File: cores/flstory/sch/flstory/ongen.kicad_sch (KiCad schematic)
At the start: 25 parts, among them M14 74LS273, M20 74LS139, M21 74LS32, M28 YM2149, M29 MSM5232RS, M33 74LS273, M34 74LS273

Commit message: jt5232: wip
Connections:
- net ~{GTWR} renamed ~{MSM}
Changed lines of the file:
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@@
 	)
 	(bus_entry
-		(at 140.335 86.36)
-		(size -2.54 2.54)
+		(at 140.335 78.74)
+		(size -2.54 -2.54)
 		(stroke
 			(width 0)
@@
 	)
 	(bus_entry
-		(at 140.335 78.74)
-		(size -2.54 2.54)
+		(at 140.335 86.36)
+		(size -2.54 -2.54)
 		(stroke
 			(width 0)
@@
 	)
 	(bus_entry
-		(at 140.335 83.82)
-		(size -2.54 2.54)
+		(at 140.335 81.28)
+		(size -2.54 -2.54)
 		(stroke
 			(width 0)
@@
 	)
 	(bus_entry
-		(at 140.335 81.28)
-		(size -2.54 2.54)
+		(at 140.335 83.82)
+		(size -2.54 -2.54)
 		(stroke
 			(width 0)
@@
 	(bus
 		(pts
-			(xy 132.715 88.9) (xy 137.795 88.9)
+			(xy 132.715 76.2) (xy 137.795 76.2)
 		)
 		(stroke
@@
 	(bus
 		(pts
-			(xy 137.795 86.36) (xy 137.795 88.9)
+			(xy 137.795 78.74) (xy 137.795 76.2)
 		)
 		(stroke
@@
 	(bus
 		(pts
-			(xy 137.795 81.28) (xy 137.795 83.82)
+			(xy 137.795 83.82) (xy 137.795 81.28)
 		)
 		(stroke
@@
 	(bus
 		(pts
-			(xy 137.795 83.82) (xy 137.795 86.36)
+			(xy 137.795 81.28) (xy 137.795 78.74)
 		)
 		(stroke
@@
 		)
 	)
-	(label "CLK4"
-		(at 140.335 91.44 0)
-		(fields_autoplaced yes)
-		(effects
-			(font
-				(size 1.27 1.27)
-			)
-			(justify left bottom)
-		)
-	)
 	(label "BASS3"
 		(at 256.54 101.6 0)
@@
 		)
 	)
-	(label "~{GTWR}"
+	(label "~{MSM}"
 		(at 140.335 88.9 0)
 		(fields_autoplaced yes)
@@
 	(hierarchical_label "SA[0..15]"
 		(shape input)
-		(at 132.715 88.9 180)
+		(at 132.715 76.2 180)
 		(fields_autoplaced yes)
 		(effects
@@
 		)
 	)
+	(hierarchical_label "CLK4"
+		(shape input)
+		(at 140.335 91.44 180)
+		(fields_autoplaced yes)
+		(effects
+			(font
+				(size 1.27 1.27)
+			)
+			(justify right)
+		)
+	)
 	(hierarchical_label "PSG"
 		(shape output)
@@
 		)
 	)
-	(hierarchical_label "~{GTWR}"
+	(hierarchical_label "~{MSM}"
 		(shape output)
 		(at 95.885 165.1 0)

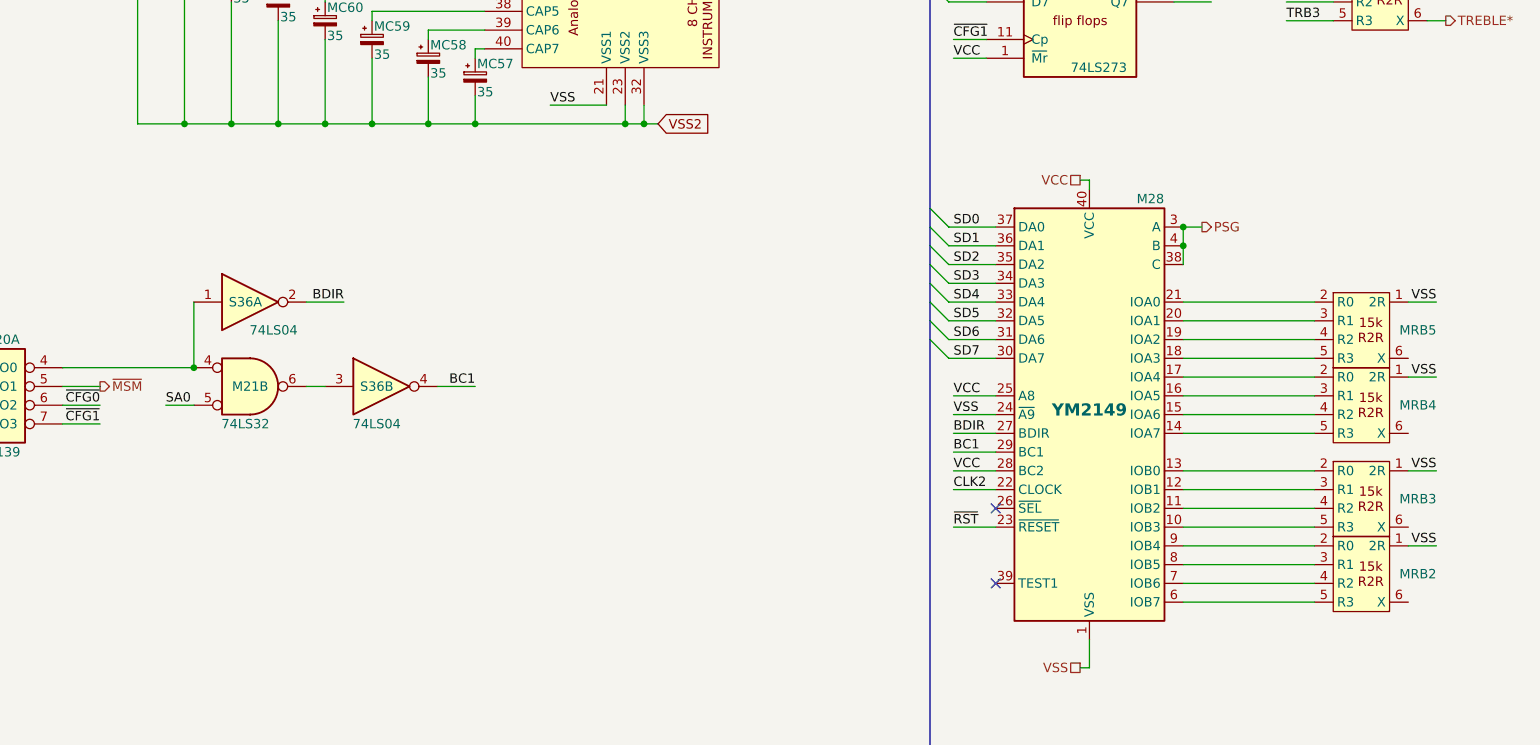
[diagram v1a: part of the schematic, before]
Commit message: flstory: TA7630 volume/balance applied
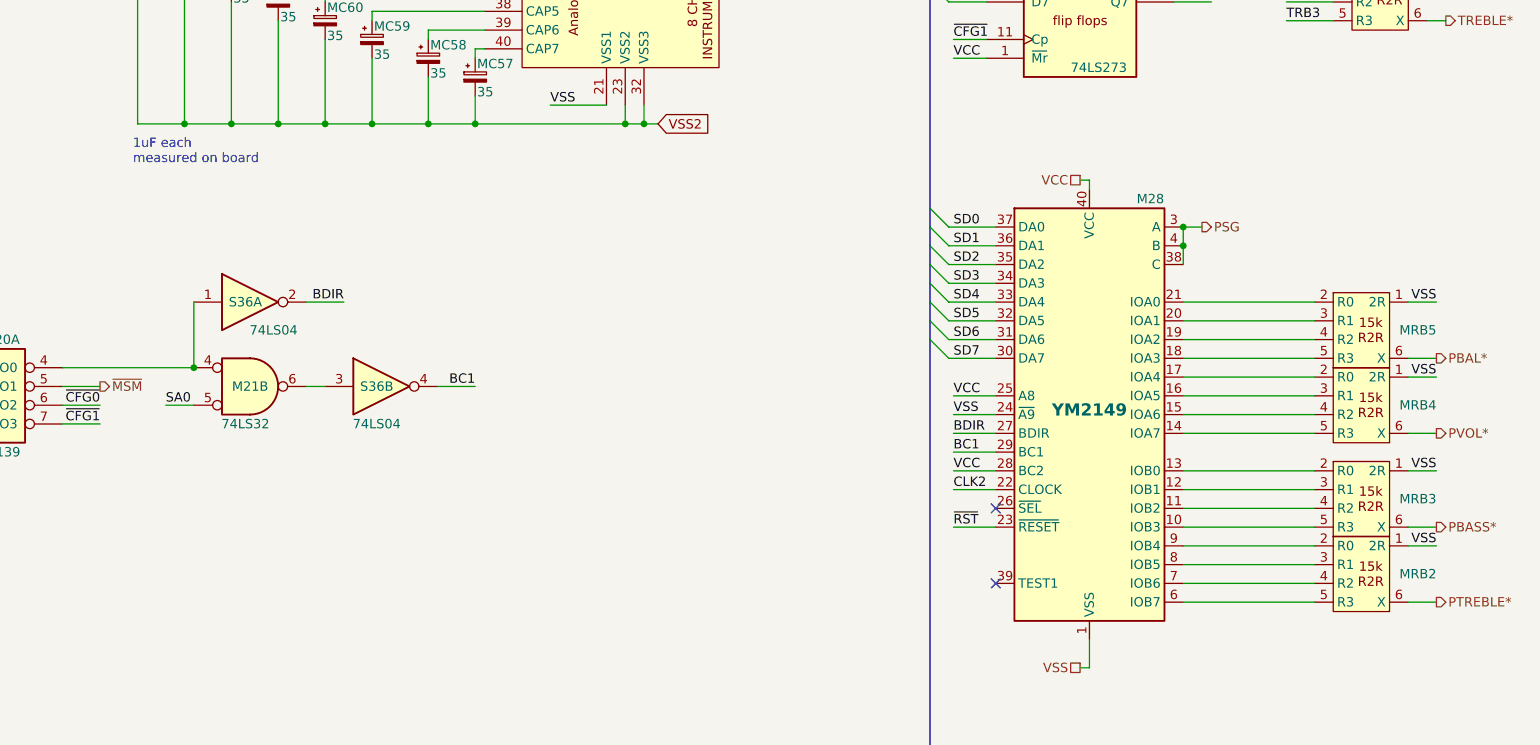
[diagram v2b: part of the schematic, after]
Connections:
- net PBAL*: now reaches MRB5.6 (X)
- net PVOL*: now reaches MRB4.6 (X)
- net PBASS*: now reaches MRB3.6 (X)
- net PTREBLE*: now reaches MRB2.6 (X)
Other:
- note added: "1uF each measured on board"
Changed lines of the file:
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@@
 	(wire
 		(pts
+			(xy 273.05 161.29) (xy 276.86 161.29)
+		)
+		(stroke
+			(width 0)
+			(type default)
+		)
+	)
+	(wire
+		(pts
 			(xy 211.455 184.15) (xy 217.17 184.15)
 		)
@@
 	(wire
 		(pts
+			(xy 273.05 171.45) (xy 276.86 171.45)
+		)
+		(stroke
+			(width 0)
+			(type default)
+		)
+	)
+	(wire
+		(pts
 			(xy 140.335 73.66) (xy 147.955 73.66)
 		)
@@
 	(wire
 		(pts
+			(xy 273.05 184.15) (xy 276.86 184.15)
+		)
+		(stroke
+			(width 0)
+			(type default)
+		)
+	)
+	(wire
+		(pts
 			(xy 242.57 189.23) (xy 260.35 189.23)
 		)
@@
 	(wire
 		(pts
+			(xy 273.05 194.31) (xy 276.86 194.31)
+		)
+		(stroke
+			(width 0)
+			(type default)
+		)
+	)
+	(wire
+		(pts
 			(xy 140.335 129.54) (xy 146.685 129.54)
 		)
@@
 		)
 	)
+	(text "1uF each\nmeasured on board"
+		(exclude_from_sim no)
+		(at 100.33 133.35 0)
+		(effects
+			(font
+				(size 1.27 1.27)
+			)
+			(justify left)
+		)
+	)
 	(label "SD4"
 		(at 215.9 68.58 180)
@@
 		)
 	)
+	(hierarchical_label "PTREBLE*"
+		(shape output)
+		(at 276.86 194.31 0)
+		(fields_autoplaced yes)
+		(effects
+			(font
+				(size 1.27 1.27)
+			)
+			(justify left)
+		)
+	)
 	(hierarchical_label "TONEA"
 		(shape output)
@@
 		)
 	)
+	(hierarchical_label "PBASS*"
+		(shape output)
+		(at 276.86 184.15 0)
+		(fields_autoplaced yes)
+		(effects
+			(font
+				(size 1.27 1.27)
+			)
+			(justify left)
+		)
+	)
 	(hierarchical_label "CLK2"
 		(shape input)
@@
 		)
 	)
+	(hierarchical_label "PVOL*"
+		(shape output)
+		(at 276.86 171.45 0)
+		(fields_autoplaced yes)
+		(effects
+			(font
+				(size 1.27 1.27)
+				(thickness 0.1588)
+			)
+			(justify left)
+		)
+	)
 	(hierarchical_label "SD[0..7]"
 		(shape bidirectional)
@@
 			)
 			(justify left)
+		)
+	)
+	(hierarchical_label "PBAL*"
+		(shape output)
+		(at 276.86 161.29 0)
+		(fields_autoplaced yes)
+		(effects
+			(font
+				(size 1.27 1.27)
+				(thickness 0.1588)
+			)
+			(justify left)

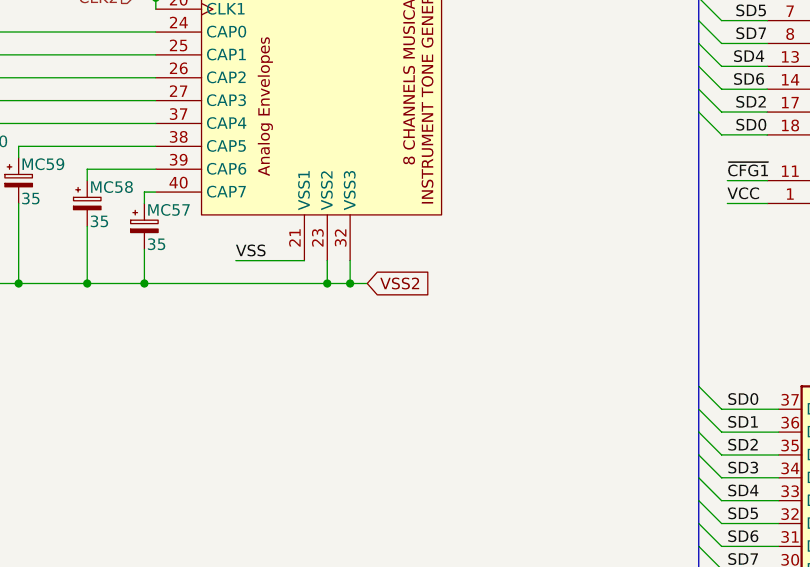
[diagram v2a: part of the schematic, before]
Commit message: flstory: sound test board
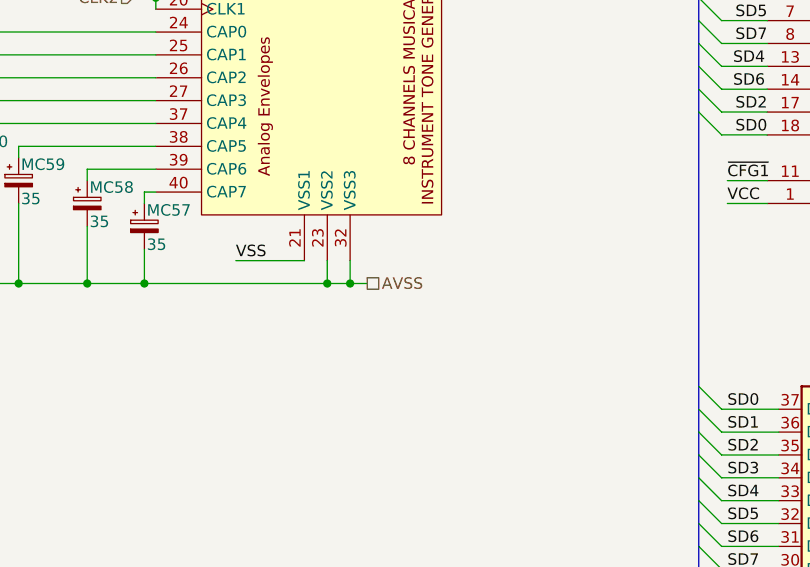
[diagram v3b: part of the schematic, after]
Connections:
- net VSS2 renamed AVSS
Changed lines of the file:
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@@
-		)
-	)
-	(global_label "VSS2"
-		(shape input)
-		(at 171.45 129.54 0)
-		(fields_autoplaced yes)
-		(effects
-			(font
-				(size 1.27 1.27)
-			)
-			(justify left)
-		)
-		(property "Intersheetrefs" "${INTERSHEET_REFS}"
-			(at 179.1523 129.54 0)
-			(effects
-				(font
-					(size 1.27 1.27)
-				)
-				(justify left)
-				(hide yes)
-			)
 		)
 	)
@@
 		(fields_autoplaced yes)
 		(effects
+			(font
+				(size 1.27 1.27)
+			)
+			(justify left)
+		)
+	)
+	(hierarchical_label "AVSS"
+		(shape passive)
+		(at 171.45 129.54 0)
+		(fields_autoplaced yes)
+		(effects
